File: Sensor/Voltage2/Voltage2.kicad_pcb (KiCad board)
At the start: 2 copper layers, 42.5 x 48.3 mm, 31 parts, among them J1 Conn_01x03_Female, J2 STX-3120-5B, J3 Conn_01x04_Female, T1 Transformer_1P_1S, U1 OPA4134

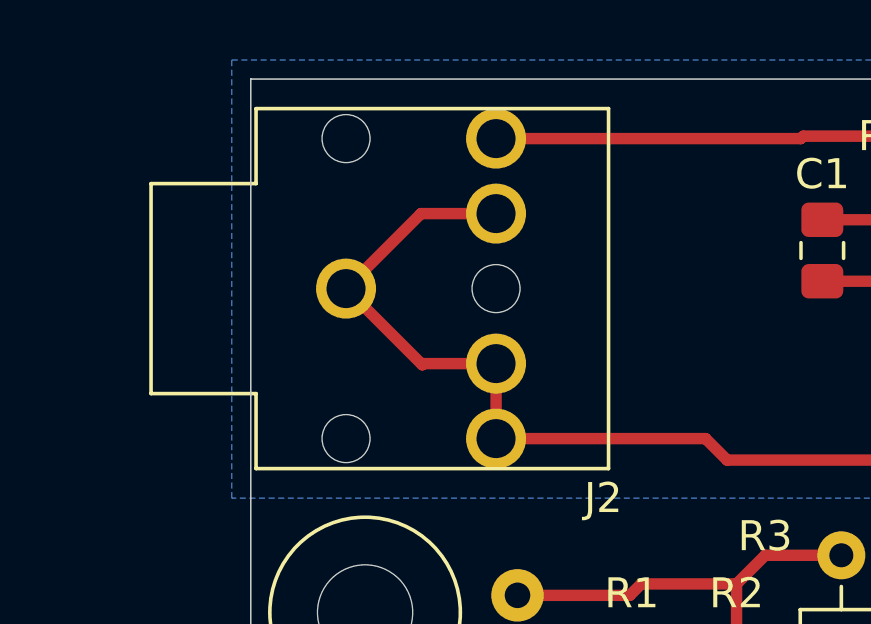
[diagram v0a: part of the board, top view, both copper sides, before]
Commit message: Fix footprint.  Fix wiring for connector.
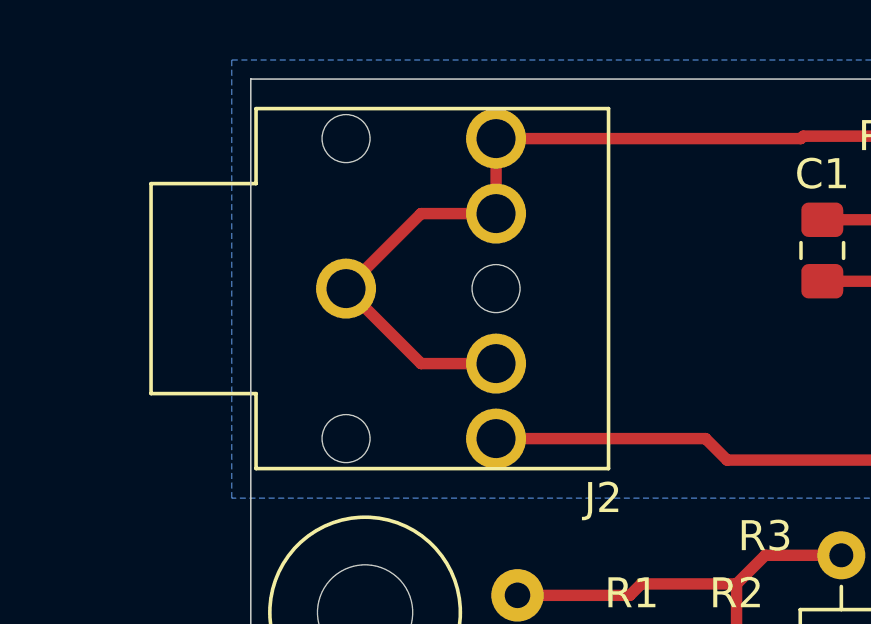
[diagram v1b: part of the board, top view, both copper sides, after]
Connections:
- J2 pad 1: /Amp+ -> /Cur+
- J2 pad 3: /Amp+ -> /Cur+
- J2 pad 4: /Amp+ -> /Cur+
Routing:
- net /Amp+: track 81.1 -> 66.5 mm
- net /Cur+: track 15.9 -> 30.5 mm
